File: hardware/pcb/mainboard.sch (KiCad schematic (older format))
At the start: 12 parts

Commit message: ADC schematic done
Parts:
- removed J?: CONN_01X05, symbol CONN_01X05
- added C?: C, symbol C
- added R? (x4): 10K, symbol R
- added U?: ADS1115IDGST, symbol ADS1115IDGST
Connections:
- net labels added: AIN0, AIN1, AIN2, AIN3
- wire segments 42 -> 57
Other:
- note added: "Default I^2C Address = 0b1001000"
- moved on the sheet: C?, Q?, R?, U?

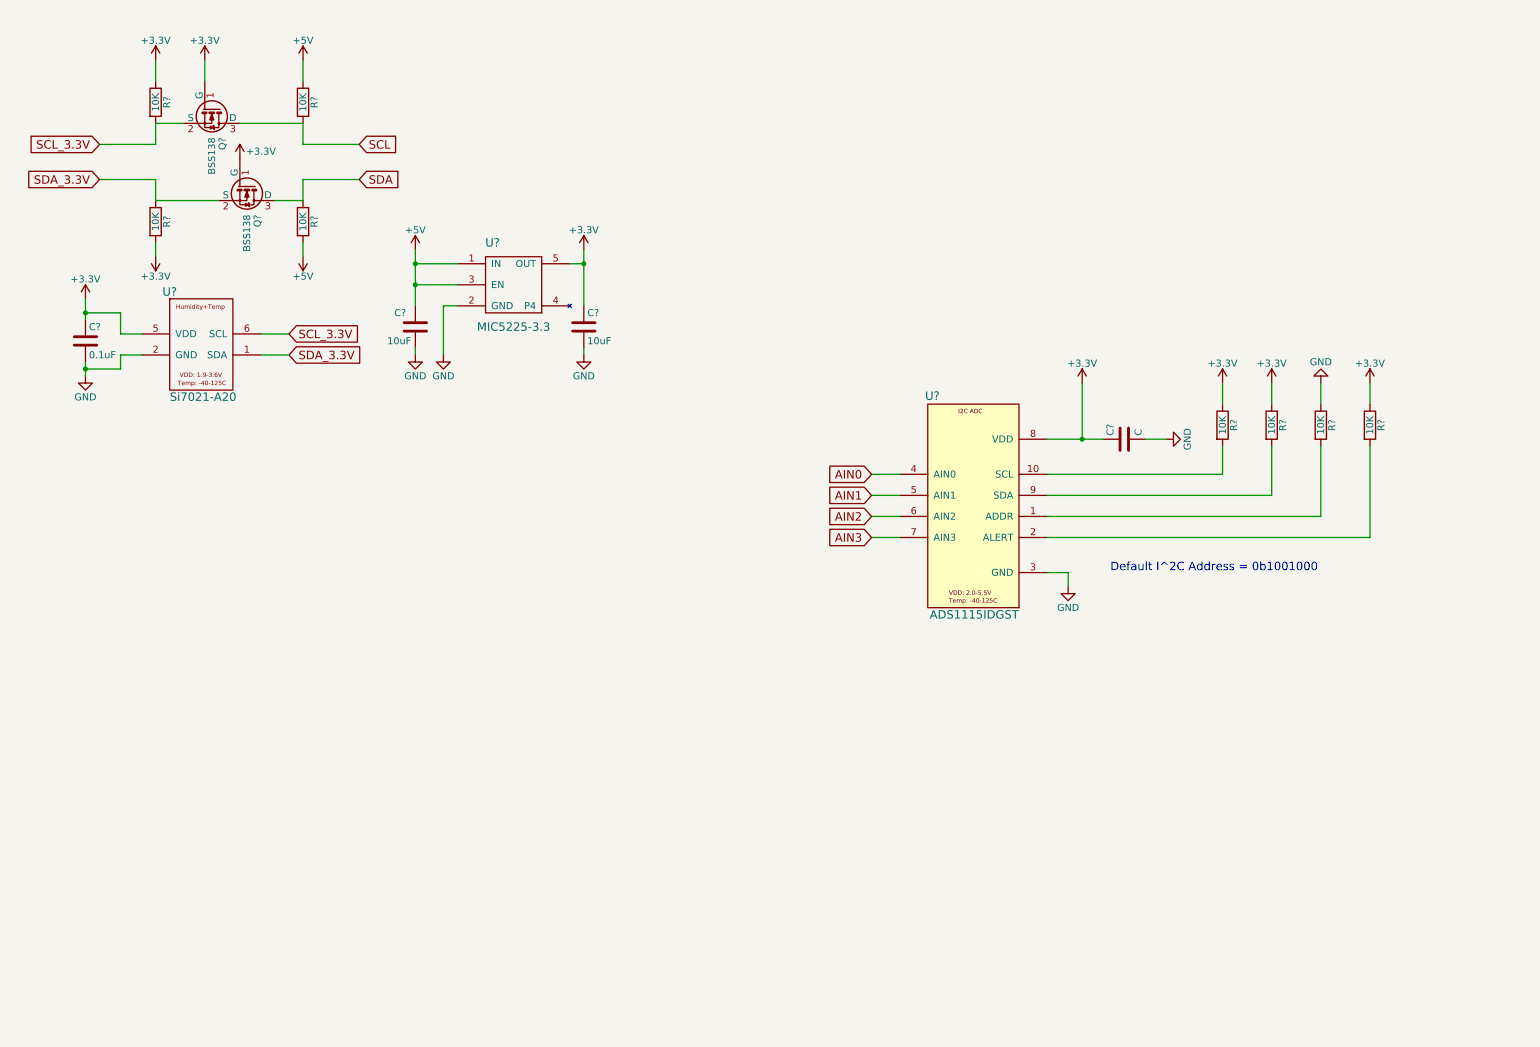
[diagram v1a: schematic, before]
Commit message: Added MICS 4514 schematic
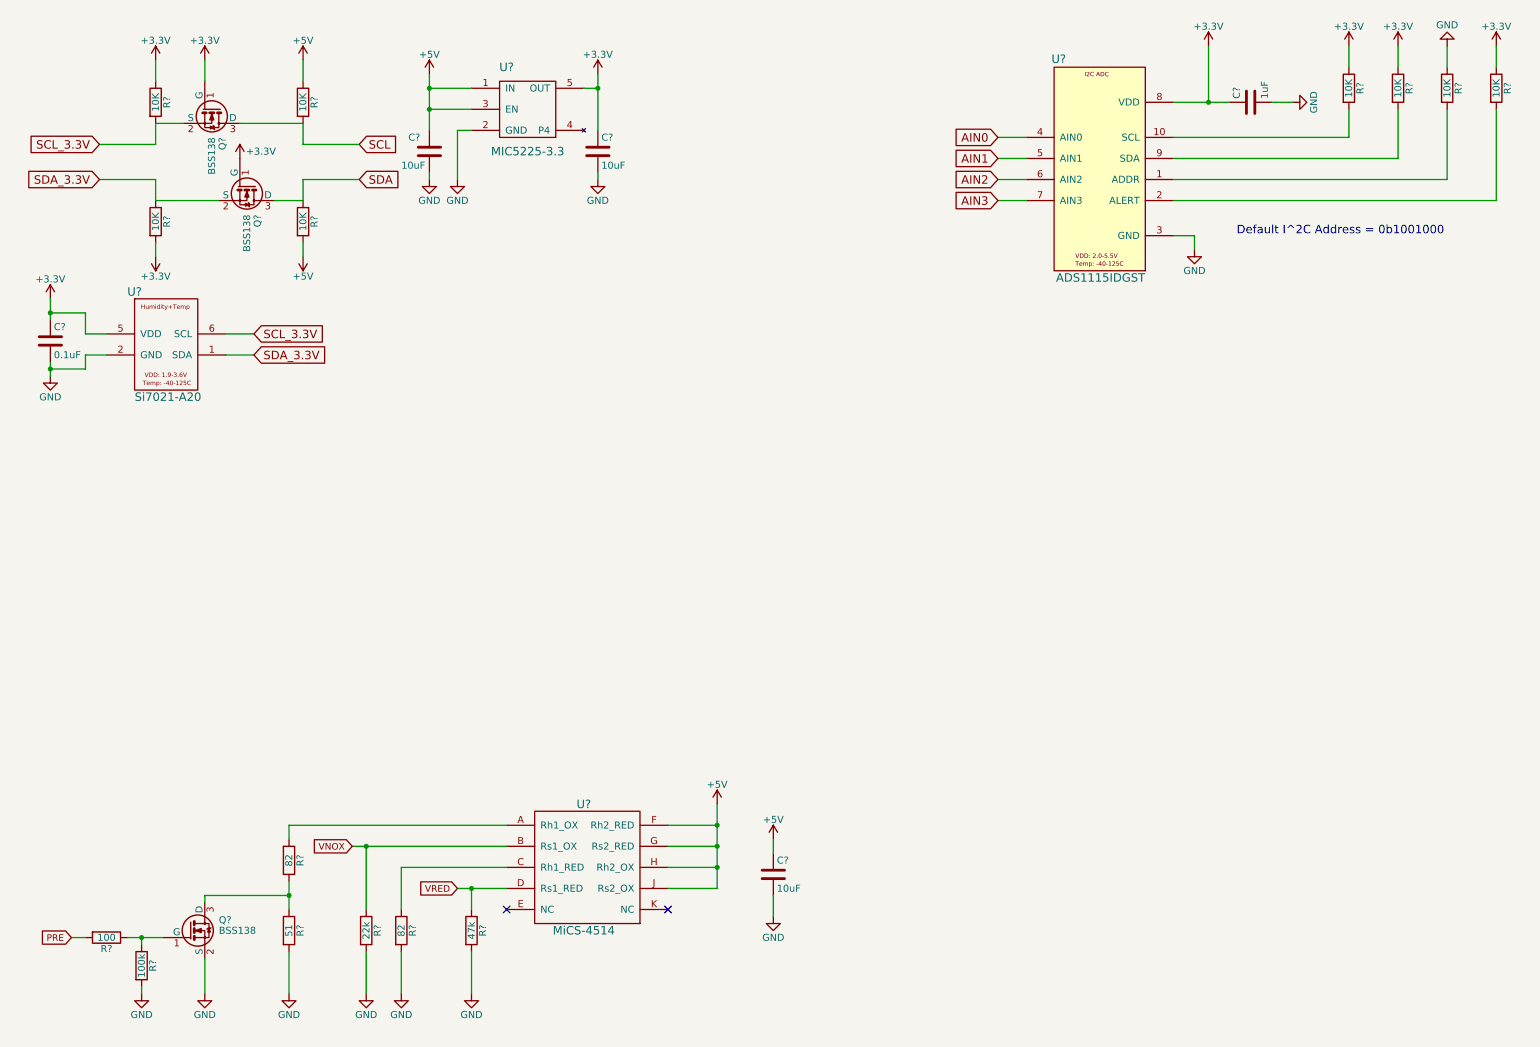
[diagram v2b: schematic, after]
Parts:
- added C?: 10uF, Capacitors_SMD:C_0805_HandSoldering, symbol C
- added Q?: BSS138, TO_SOT_Packages_SMD:SOT-23_Handsoldering, symbol BSS138
- added R? (x2): 82, Resistors_SMD:R_0805_HandSoldering, symbol R
- added R?: 51, Resistors_SMD:R_0603_HandSoldering, symbol R
- added R?: 100k, Resistors_SMD:R_0603_HandSoldering, symbol R
- added R?: 100, Resistors_SMD:R_0603_HandSoldering, symbol R
- added R?: 47k, Resistors_SMD:R_0603_HandSoldering, symbol R
- added R?: 22k, Resistors_SMD:R_0603_HandSoldering, symbol R
- added U?: MiCS-4514, MiCS-4514:MICS-4514, symbol MiCS-4514
- C?: value C -> 1uF
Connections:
- net +5V: now also C?.1, U?.F (Rh2_RED), U?.G (Rs2_RED), U?.H (Rh2_OX), U?.J (Rs2_OX)
- net GND: now also C?.2, Q?.2 (S), R?.2, R?.2, R?.2, R?.2, R?.2
- new net: R?.2, U?.A (Rh1_OX)
- new net: R?.1, U?.C (Rh1_RED)
- new net: Q?.3 (D), R?.1, R?.1
- new net: Q?.1 (G), R?.1, R?.1
- new net PRE: R?.2
- new net VNOX: R?.1, U?.B (Rs1_OX)
- new net VRED: R?.1, U?.D (Rs1_RED)
- no-connect marks 0 -> 2
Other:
- moved on the sheet: C?, R?, U?

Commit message: started om mcu
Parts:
- removed U?: MIC5225-3.3, symbol MIC5225-3.3
- added U?: MIC5225-3.3, symbol MIC5225-3.3
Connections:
- net +3V3: now also U?.5 (OUT)
- net +5V: now also U?.1 (IN), U?.3 (EN)
- net GND: now also U?.2 (GND)
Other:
- moved on the sheet: C?, Q?, R?, U?

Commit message: Working on Radio and arm m0
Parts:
- added C?: 1uF, symbol C
- added C? (x2): 22pF, symbol C
- added C?: 10uF, symbol C
- added U?: ATSAMD21G18_QFN, symbol ATSAMD21G18_QFN
- added U?: RFM95, symbol RFM95
- added Y?: 32.768, symbol Crystal
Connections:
- net +3V3: now also C?.1, U?.13 (3.3V), U?.17 (VDDIO), U?.36 (VDDIO), U?.44 (VDDIN), U?.6 (VDDANA)
- net GND: now also C?.1, C?.1, C?.1, C?.2, U?.1 (GND), U?.10 (GND), U?.18 (GND), U?.35 (GND), U?.42 (GND), U?.5 (GNDANA), U?.8 (GND)
- new net: C?.2, U?.1 (PA00), Y?.2
- new net: C?.2, U?.2 (PA01), Y?.1
- new net: C?.2, U?.43 (VDDCORE)
- new net D3_IRQ: U?.14 (DIO0)
- new net D4_RST: U?.6 (RESET)
- new net D8_CS: U?.5 (NSS)
- new net DIO1: U?.15 (DIO1)
- new net DIO2: U?.16 (DIO2)
- new net DIO3: U?.11 (DIO3)
- new net DIO5: U?.7 (DIO5)
- new net MISO: U?.2 (MISO)
- new net MOSI: U?.3 (MOSI)
- new net SCK: U?.4 (SCK)
- no-connect marks 2 -> 3

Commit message: more work on pcb
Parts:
- added D?: LED, symbol LED
- added R?: R, symbol R
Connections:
- net D3_IRQ: now also U?.14 (PA09)
- net D4_RST: now also U?.13 (PA08)
- net D8_CS: now also U?.11 (PA06)
- net GND: now also D?.1 (K)
- net MISO: now also U?.21 (PA12)
- net MOSI: now also U?.19 (PB10)
- net SCK: now also U?.20 (PB11)
- net D13: now reaches U?.26 (PA17)
- net D13: now also R?.1
- new net: D?.2 (A), R?.2
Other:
- note added: "2018"
- note added: "DAJB\n"
- note added: "Pollution Sensor with Cortex M0+ and RFM95\n"
- note added: "v1.0"
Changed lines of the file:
@@
 DIO3
 NoConn ~ 6200 4700
+$Comp
+L R R?
+U 1 1 5A7C8589
+P 2800 4550
+F 0 "R?" V 2880 4550 50  0000 C CNN
+F 1 "R" V 2800 4550 50  0000 C CNN
+F 2 "" V 2730 4550 50  0001 C CNN
+F 3 "" H 2800 4550 50  0001 C CNN
+	1    2800 4550
+	1    0    0    -1
+$EndComp
+$Comp
+L LED D?
+U 1 1 5A7C85E4
+P 2800 5000
+F 0 "D?" H 2800 5100 50  0000 C CNN
+F 1 "LED" H 2800 4900 50  0000 C CNN
+F 2 "" H 2800 5000 50  0001 C CNN
+F 3 "" H 2800 5000 50  0001 C CNN
+	1    2800 5000
+	0    -1   -1   0
+$EndComp
+Wire Wire Line
+	2800 4850 2800 4700
+$Comp
+L GND #PWR?
+U 1 1 5A7C8759
+P 2800 5350
+F 0 "#PWR?" H 2800 5100 50  0001 C CNN
+F 1 "GND" H 2800 5200 50  0000 C CNN
+F 2 "" H 2800 5350 50  0001 C CNN
+F 3 "" H 2800 5350 50  0001 C CNN
+	1    2800 5350
+	1    0    0    -1
+$EndComp
+Wire Wire Line
+	2800 5350 2800 5150
+Wire Wire Line
+	2800 4400 2800 4300
+Text GLabel 2800 4300 1    51   Input ~ 0
+D13
+Text GLabel 10100 4900 2    51   Input ~ 0
+D13
+Text GLabel 8600 5450 3    51   Input ~ 0
+D3_IRQ
+Text GLabel 8500 5450 3    51   Input ~ 0
+D4_RST
+Text GLabel 9200 5450 3    51   Input ~ 0
+SCK
+Text GLabel 9100 5450 3    51   Input ~ 0
+MOSI
+Text GLabel 9300 5450 3    51   Input ~ 0
+MISO
+Text GLabel 8000 4900 0    51   Input ~ 0
+D8_CS
+Text Notes 8140 7640 0    51   ~ 0
+2018
+Text Notes 10630 7630 0    51   ~ 0
+v1.0
+Text Notes 7350 7500 0    51   ~ 0
+Pollution Sensor with Cortex M0+ and RFM95\n
+Text Notes 10950 7490 0    51   ~ 0
+DAJB\n
 $EndSCHEMATC

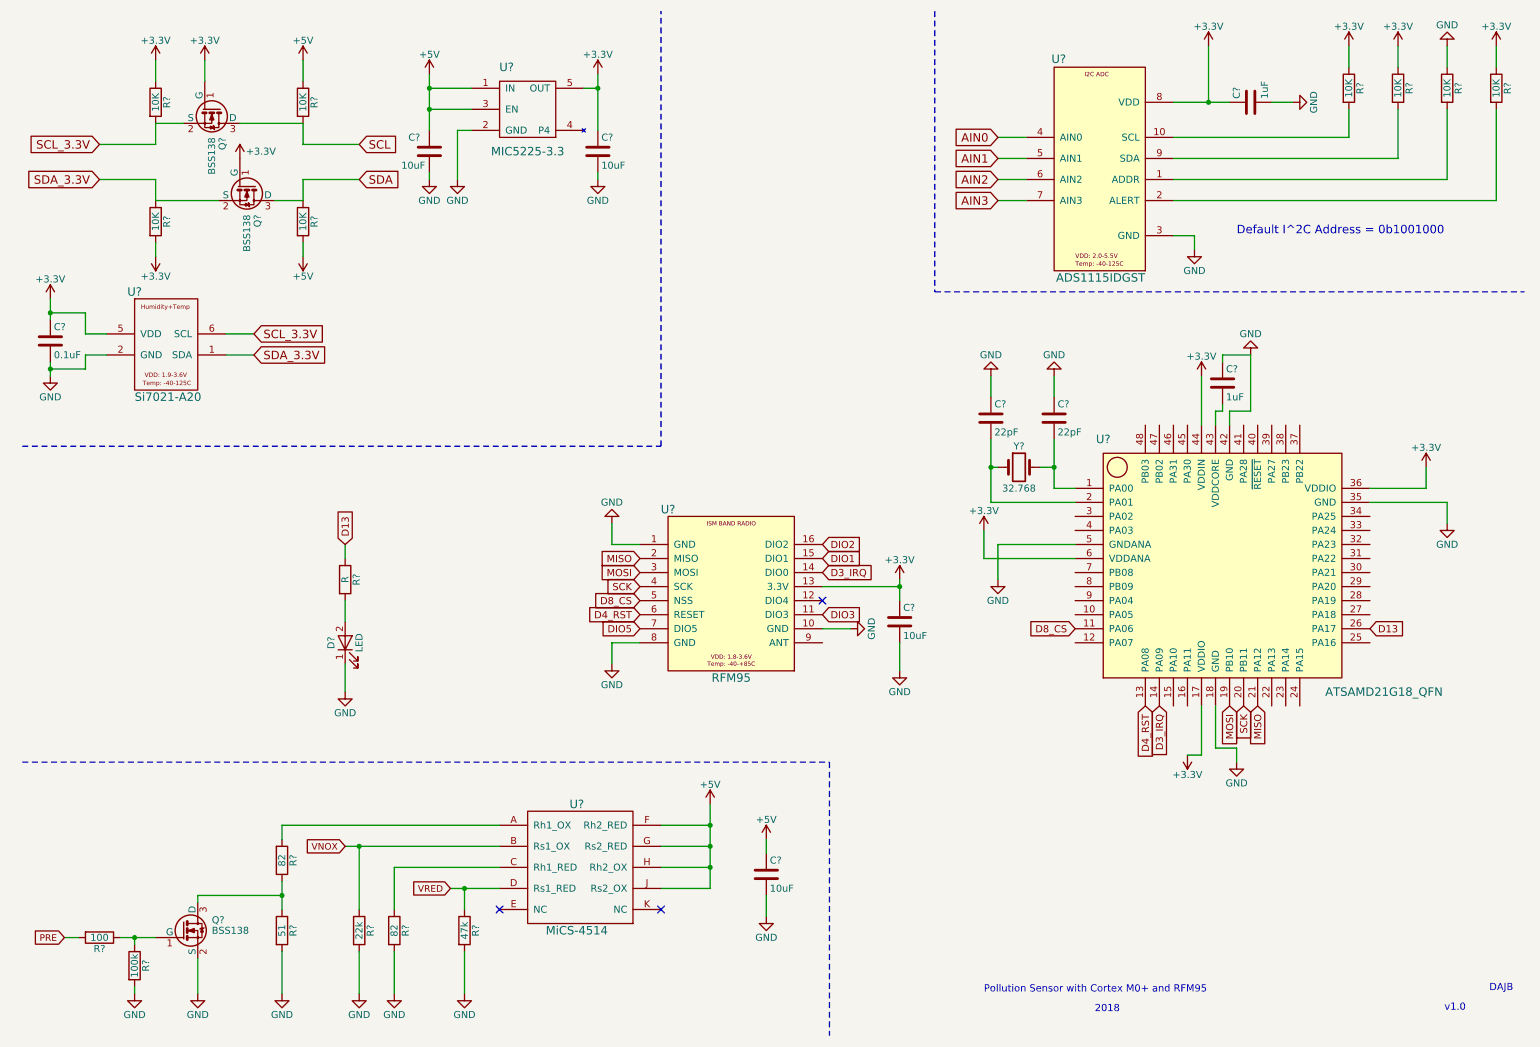
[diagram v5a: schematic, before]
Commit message: More pcb work and website hosted on rpi
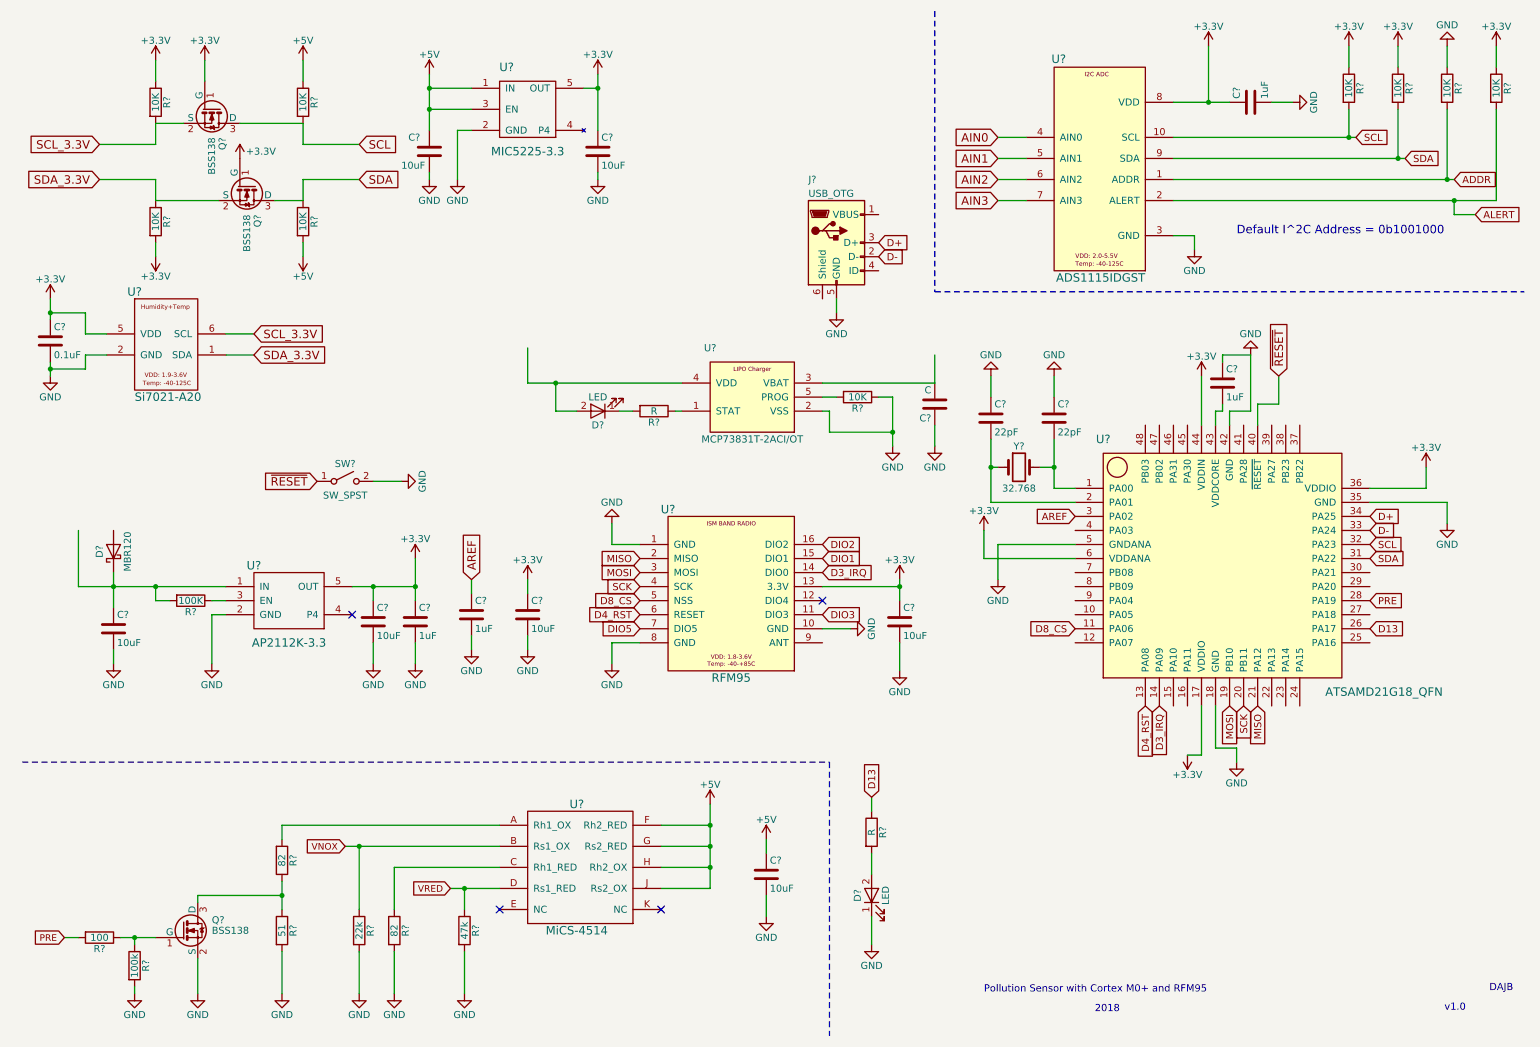
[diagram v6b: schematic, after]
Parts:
- added C?: 10uF, Capacitors_SMD:C_0805_HandSoldering, symbol C
- added C?: 1uF, Capacitors_SMD:C_0805_HandSoldering, symbol C
- added C?: 1uF, symbol C
- added C? (x2): 10uF, symbol C
- added C?: C, symbol C
- added D?: LED, symbol LED
- added D?: MBR120, symbol D_Schottky
- added J?: USB_OTG, symbol USB_OTG
- added R?: 100K, symbol R
- added R?: R, symbol R
- added R?: 10K, symbol R
- added SW?: SW_SPST, symbol SW_SPST
- added U?: AP2112K-3.3, symbol AP2112K-3.3
- added U?: MCP73831T-2ACI/OT, symbol MCP73831T-2ACI/OT
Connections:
- net +3V3: now also C?.1, C?.1, C?.1, U?.5 (OUT)
- net GND: now also C?.1, C?.2, C?.2, C?.2, C?.2, C?.2, J?.5 (GND), R?.1, SW?.2 (B), U?.2 (GND), U?.2 (VSS)
- net PRE: now also U?.28 (PA19)
- net SCL: now also R?.2, U?.10 (SCL), U?.32 (PA23)
- net SDA: now also R?.2, U?.31 (PA22), U?.9 (SDA)
- net ADDR: now reaches R?.2, U?.1 (ADDR)
- net ALERT: now reaches R?.2, U?.2 (ALERT)
- net AREF: now reaches U?.3 (PA02)
- net AREF: now also C?.1
- net D-: now reaches U?.33 (PA24)
- net D-: now also J?.2 (D-)
- net D+: now reaches U?.34 (PA25)
- net D+: now also J?.3 (D+)
- net ~RESET: now reaches U?.40 (~RESET)
- net ~RESET: now also SW?.1 (A)
- new net: C?.1, D?.1 (K), R?.2, U?.1 (IN)
- new net: R?.1, U?.3 (EN)
- new net: R?.1, U?.1 (STAT)
- new net: C?.2, U?.3 (VBAT)
- new net: D?.2 (A), U?.4 (VDD)
- new net: R?.2, U?.5 (PROG)
- new net: D?.1 (K), R?.2
- no-connect marks 3 -> 4
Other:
- moved on the sheet: D?, R?
